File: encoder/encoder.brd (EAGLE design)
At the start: 44.1 x 12.7 mm, 8 parts, among them U1 AH_3761, U2 AH_3761

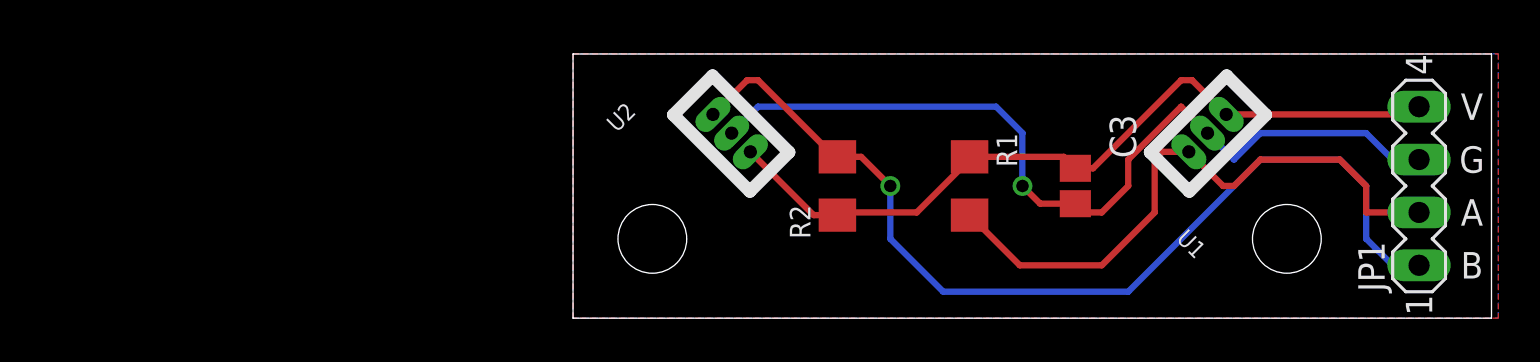
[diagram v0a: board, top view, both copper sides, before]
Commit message: Resolve stop mask errors with encoder.
Change-Id: I9fddeda359ca22c296966b7b0eabcc96fce67350
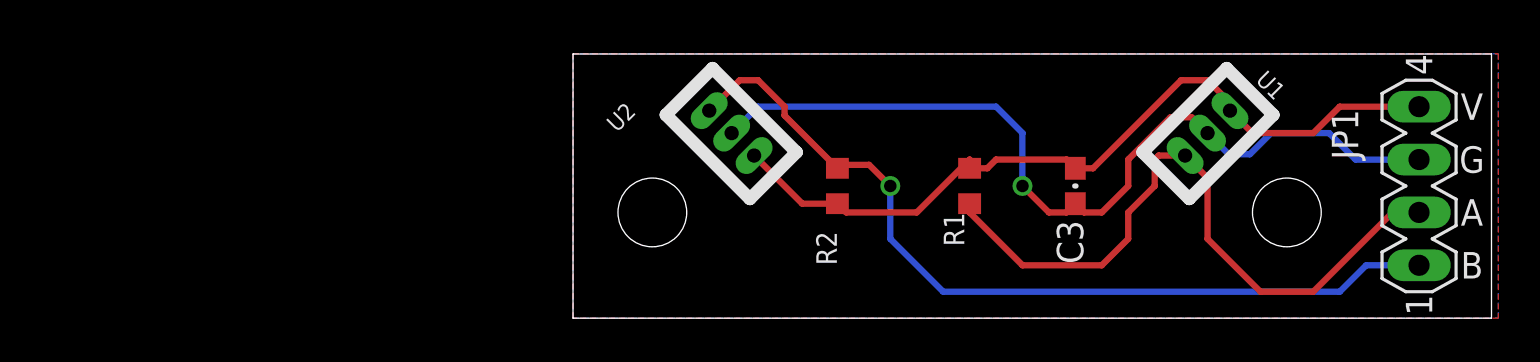
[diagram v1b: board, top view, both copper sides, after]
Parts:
- C3: device resistor:C2012 -> pie:0603-CAP
- R1, R2: device resistor:R3216 -> pie:R0603
- moved E$1 1.27 mm to (59.7, 5.08)
- moved E$2 1.27 mm to (29.2, 5.08)
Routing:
- net OUT2: track 46.7 -> 41.3 mm
- net OUT1: track 29.3 -> 32.7 mm
- net VCC: track 37.4 -> 38.4 mm

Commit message: Fix silk and use MTA100 on encoder
Change-Id: I97656cb59db7609cb5a5fb3d273ef94f8a7b6129
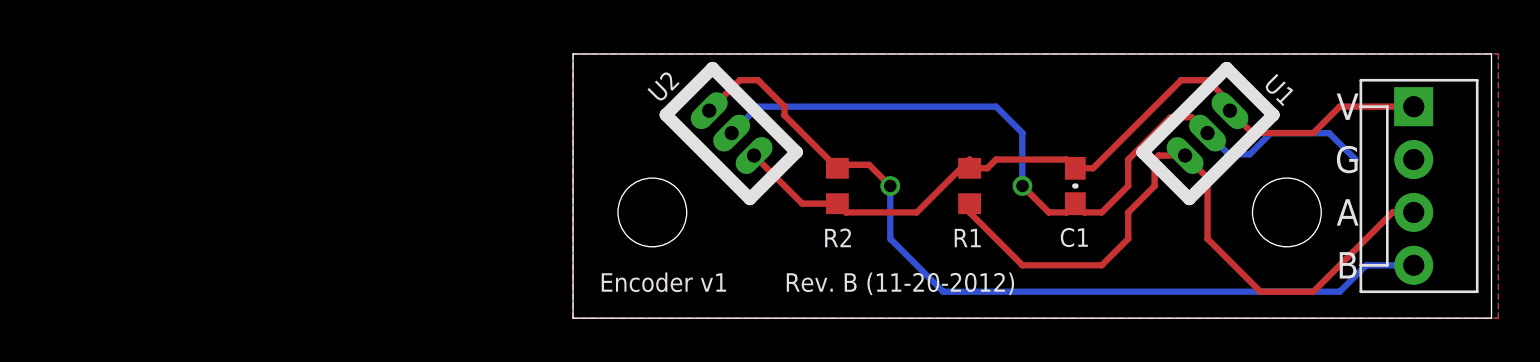
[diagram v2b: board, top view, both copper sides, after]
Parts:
- added U$1: (no value), pie:PIE-LOGO-SMALL
- JP1: device con-lstb:MA04-1 -> pie:MOLEX-1X4
- moved JP1 3.82 mm to (65.8, 10.2), turned to 270 degrees
- renumbered C3 to C1
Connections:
- net GND: now also JP1.2; no longer JP1.3
- net OUT1: now also JP1.3; no longer JP1.2
- net OUT2: now also JP1.4; no longer JP1.1
- net VCC: now also JP1.1; no longer JP1.4
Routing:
- net GND: track 41.8 -> 38.8 mm
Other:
- board text added: "Encoder v1"
- board text added: "Rev. B (11-20-2012)"

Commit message: Fix all boards to be at origin, fix dimension width to be 10 mil
Change-Id: I08bc507f450d0f63cfcc98eecb1f52bd6fb958a5
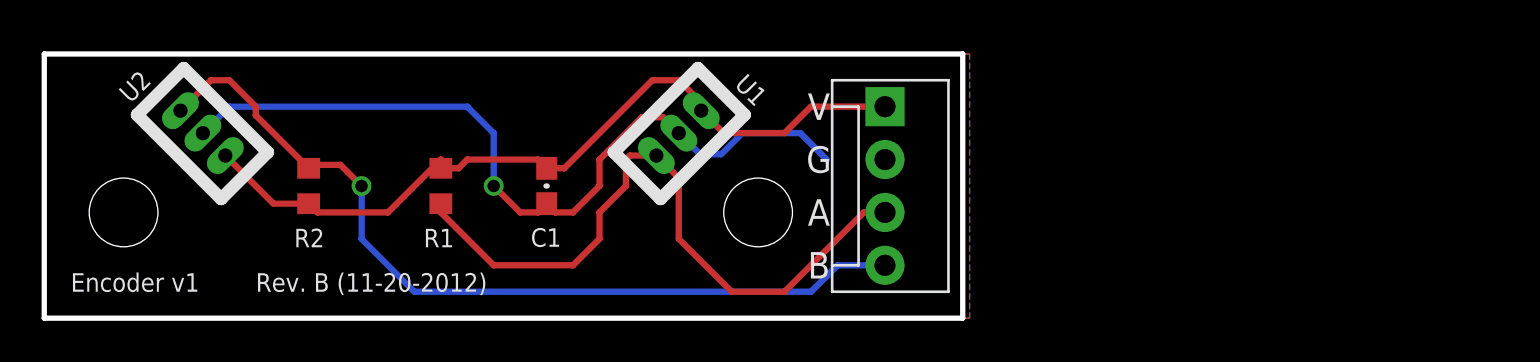
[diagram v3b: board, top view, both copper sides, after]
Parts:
- moved C1 25.4 mm to (24.1, 6.35)
- moved E$2 25.4 mm to (3.81, 5.08)
- moved R1 25.4 mm to (19.1, 6.35)
- moved R2 25.4 mm to (12.7, 6.35)
- moved U$1 25.4 mm to (21.6, 6.35)
- moved U1 25.4 mm to (30.5, 8.89)
- moved U2 25.4 mm to (7.62, 8.89)
- moved E$1 25.4 mm to (34.3, 5.08)
- moved JP1 25.4 mm to (40.4, 10.2)

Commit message: added copyright stuff and open source logo
Change-Id: Ia149b3f1e75c81f992df6b9b6b68b519a3d9cc7f
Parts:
- added U$2: (no value), pie:OSHW-LOGO-S
- moved U$1 8.01 mm to (13.6, 6.73)
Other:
- board text added: "Copyright (c) 2013, Pioneers in Engineering All rights reserved. Design by: Chris Buonocore This design is open source hardware. For more information, visit pioneers.berkeley.edu/opensource"
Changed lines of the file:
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@@
 <?xml version="1.0" encoding="utf-8"?>
 <!DOCTYPE eagle SYSTEM "eagle.dtd">
-<eagle version="6.2">
+<eagle version="6.3">
 <drawing>
 <settings>
@@
 <layer number="107" name="Crop" color="7" fill="1" visible="no" active="yes"/>
 <layer number="108" name="Extra" color="7" fill="1" visible="no" active="yes"/>
+<layer number="109" name="fp9" color="7" fill="1" visible="yes" active="yes"/>
+<layer number="110" name="fp0" color="7" fill="1" visible="yes" active="yes"/>
 <layer number="116" name="Patch_BOT" color="9" fill="4" visible="no" active="yes"/>
 <layer number="121" name="_tsilk" color="7" fill="1" visible="no" active="yes"/>
 <layer number="122" name="_bsilk" color="7" fill="1" visible="no" active="yes"/>
+<layer number="123" name="tTestmark" color="7" fill="1" visible="yes" active="yes"/>
+<layer number="124" name="bTestmark" color="7" fill="1" visible="yes" active="yes"/>
 <layer number="125" name="_tNames" color="7" fill="1" visible="no" active="yes"/>
+<layer number="131" name="tAdjust" color="7" fill="1" visible="yes" active="yes"/>
+<layer number="132" name="bAdjust" color="7" fill="1" visible="yes" active="yes"/>
 <layer number="144" name="Drill_legend" color="7" fill="1" visible="no" active="yes"/>
 <layer number="151" name="HeatSink" color="7" fill="1" visible="no" active="yes"/>
@@
 <text x="1.27" y="1.27" size="0.889" layer="21" font="vector" ratio="20">Encoder v1</text>
 <text x="10.16" y="1.27" size="0.889" layer="21" font="vector" ratio="20">Rev. B (11-20-2012)</text>
+<text x="31.75" y="1.27" size="0.4064" layer="22" font="vector" rot="MR0">Copyright (c) 2013, Pioneers in Engineering
+All rights reserved.
+Design by: Chris Buonocore
+This design is open source hardware.
+For more information, visit pioneers.berkeley.edu/opensource</text>
 </plain>
 <attributes>
@@
 </class>
 </classes>
-<designrules>
+<designrules name="default">
 <description language="de">&lt;b&gt;EAGLE Design Rules&lt;/b&gt;
 &lt;p&gt;
@@
 <element name="E$2" library="SparkFun-Electromechanical" package="STAND-OFF" value="" x="3.81" y="5.08"/>
 <element name="JP1" library="pie" package="MOLEX-1X4" value="" x="40.386" y="10.16" rot="R270"/>
-<element name="U$1" library="pie" package="PIE-LOGO-SMALL" value="" x="21.59" y="6.35" rot="MR0"/>
+<element name="U$1" library="pie" package="PIE-LOGO-SMALL" value="" x="13.589" y="6.731" rot="MR0"/>
+<element name="U$2" library="pie" package="OSHW-LOGO-S" value="" x="25.4" y="10.16" rot="MR0"/>
 </elements>
 <signals>
@@
 </board>
 </drawing>
+<compatibility>
+<note version="6.3" minversion="6.2.2" severity="warning">
+Since Version 6.2.2 text objects can contain more than one line,
+which will not be processed correctly with this version.
+</note>
+</compatibility>
 </eagle>

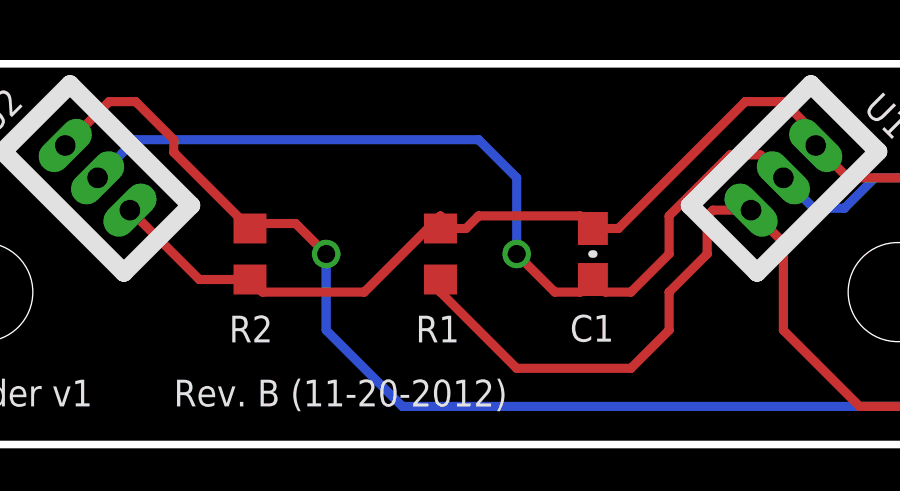
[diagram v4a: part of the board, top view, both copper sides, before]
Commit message: Made copyright readable
Change-Id: Ied6938a07163fe6dfe38c6fa4825a8684fe6fe2e
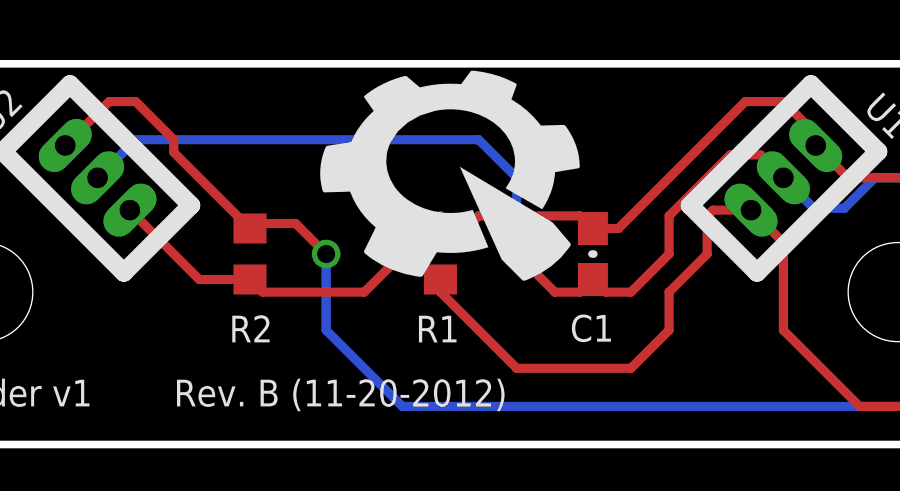
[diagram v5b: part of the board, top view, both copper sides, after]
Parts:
- moved U$1 6.60 mm to (19.7, 9.27), flipped to the top
- moved U$2 1.80 mm to (25.7, 8.38)
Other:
- board text added: "All rights reserved."
- board text added: "Copyright (c) 2013, Pioneers in Engineering"
- board text added: "Designed by: Chris Buonocore"
- board text added: "This design is open source hardware."
- board text added: "pioneers.berkeley.edu/opensource"
- board text removed: "Copyright (c) 2013, Pioneers in Engineering All rights reserved. Design by: Chris Buonocore This design is open source hardware. For more information, visit pioneers.berkeley.edu/opensource"
